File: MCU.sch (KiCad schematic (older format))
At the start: 10 parts, among them J2 Conn_01x02, J5 Conn_02x03_Odd_Even, SW2 SW_SPDT, U3 ATTINY13-20SSU

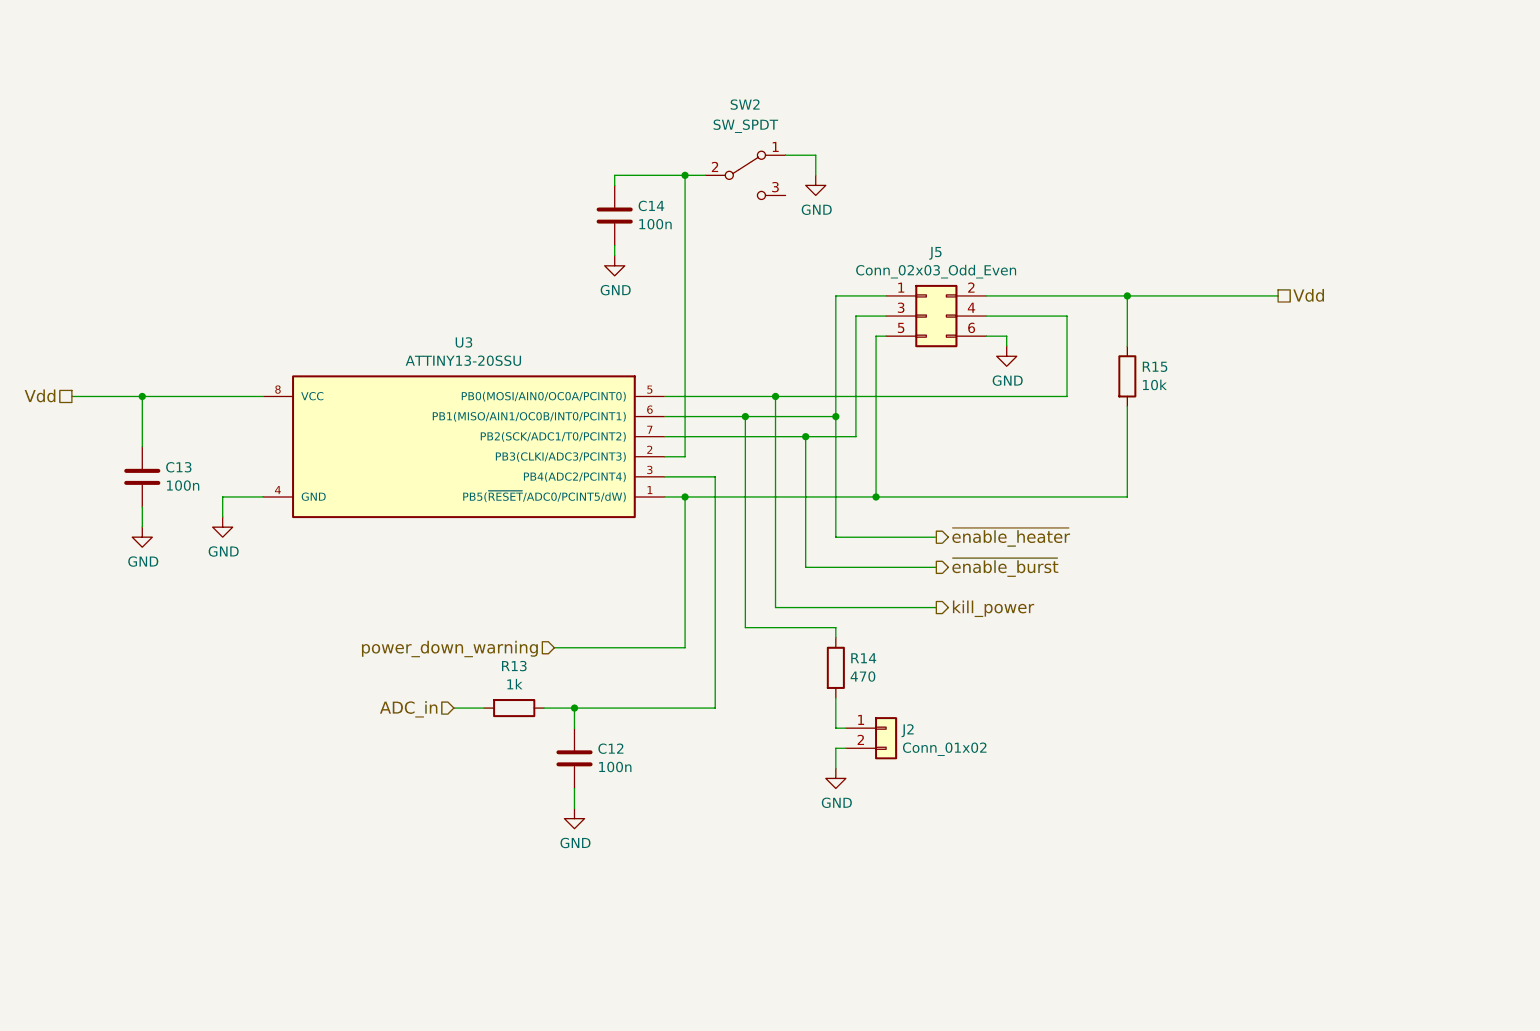
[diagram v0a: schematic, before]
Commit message: Fixed NTLJF3117P MOSFET pin layout
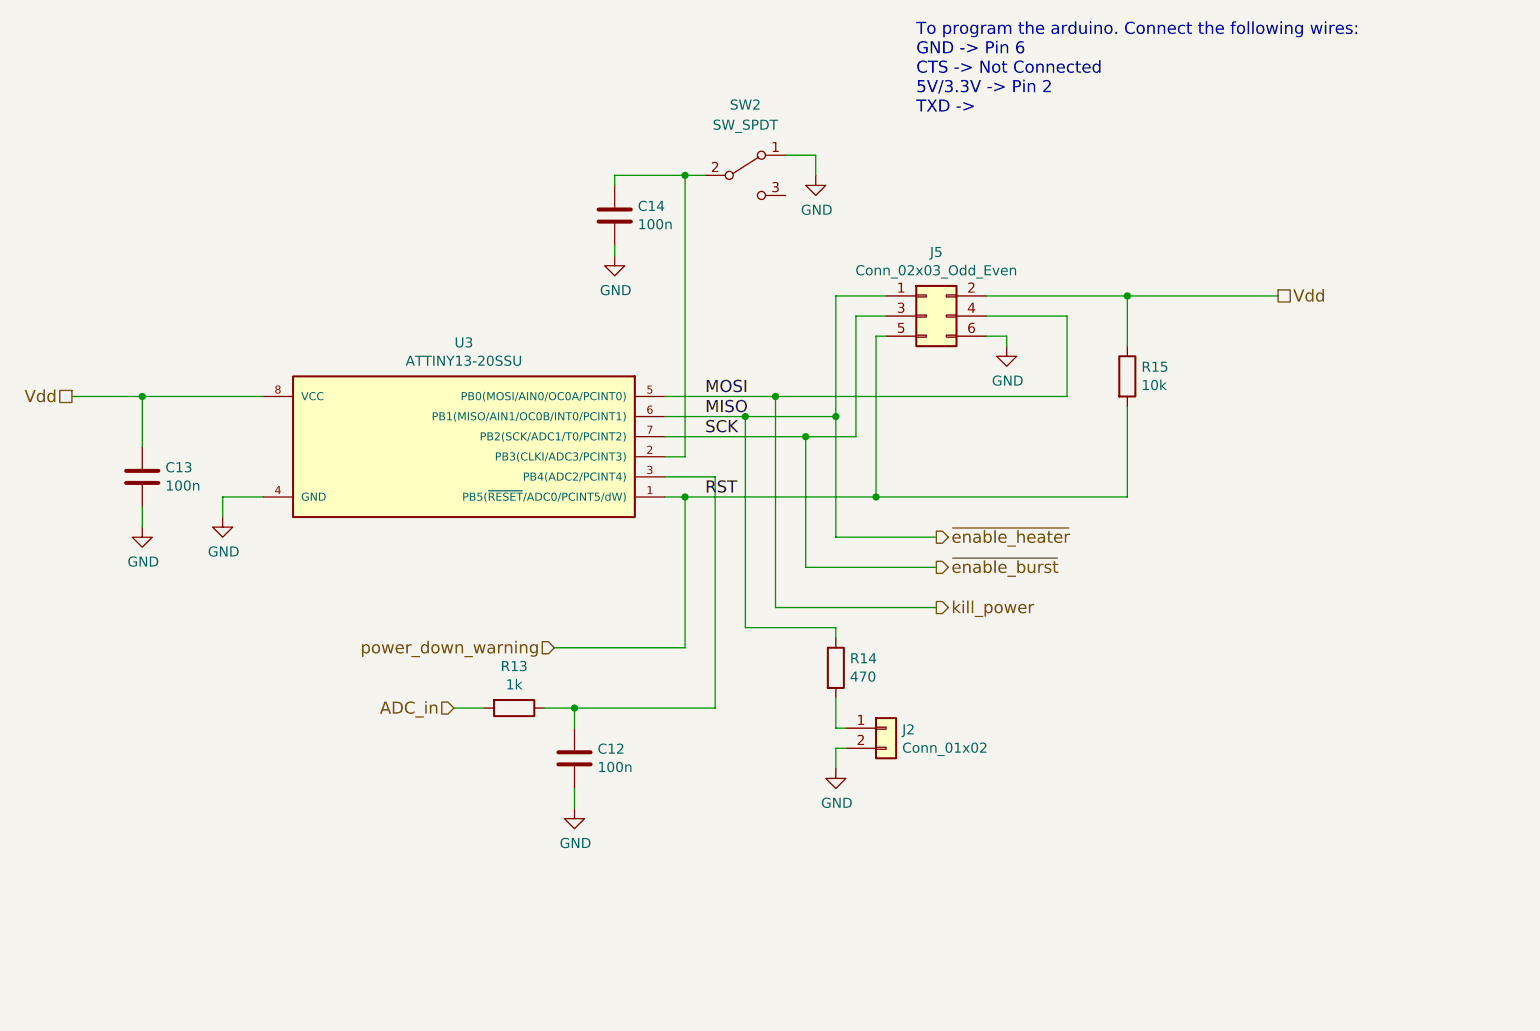
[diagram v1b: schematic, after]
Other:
- note added: "To program the arduino. Connect the following wires:\nGND -> Pin 6\nCTS -> Not Connected\n5V/3.3V -> Pin 2\nTXD ->"
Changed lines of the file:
@@
 $EndComp
 $Comp
-L GND #PWR028
+L GND #PWR027
 U 1 1 59D0B8EA
 P 5850 5050
-F 0 "#PWR028" H 5850 4800 50  0001 C CNN
+F 0 "#PWR027" H 5850 4800 50  0001 C CNN
 F 1 "GND" H 5855 4877 50  0000 C CNN
 F 2 "" H 5850 5050 50  0001 C CNN
@@
 	1    0    0    -1
 $EndComp
-Wire Wire Line
-	5250 4550 5400 4550
-Wire Wire Line
-	5700 4550 6550 4550
-Wire Wire Line
-	5850 4550 5850 4650
-Wire Wire Line
-	5850 4950 5850 5050
 $Comp
 L ATTINY13-20SSU U3
@@
 $EndComp
 $Comp
-L GND #PWR029
+L GND #PWR028
 U 1 1 59D0C06D
 P 4100 3600
-F 0 "#PWR029" H 4100 3350 50  0001 C CNN
+F 0 "#PWR028" H 4100 3350 50  0001 C CNN
 F 1 "GND" H 4105 3427 50  0000 C CNN
 F 2 "" H 4100 3600 50  0001 C CNN
@@
 	1    0    0    -1
 $EndComp
-Wire Wire Line
-	4300 3000 3350 3000
-Wire Wire Line
-	4300 3500 4100 3500
-Wire Wire Line
-	4100 3500 4100 3600
 $Comp
 L Conn_02x03_Odd_Even J5
@@
 	1    0    0    -1
 $EndComp
-Wire Wire Line
-	7400 2500 7150 2500
-Wire Wire Line
-	7150 2500 7150 3700
-Wire Wire Line
-	6300 3100 7150 3100
-Wire Wire Line
-	7400 2600 7250 2600
-Wire Wire Line
-	7250 2600 7250 3200
-Wire Wire Line
-	7250 3200 6300 3200
-Wire Wire Line
-	7400 2700 7350 2700
-Wire Wire Line
-	7350 2700 7350 3500
-Wire Wire Line
-	6300 3500 8600 3500
-Wire Wire Line
-	6300 3000 8300 3000
-Wire Wire Line
-	8300 3000 8300 2600
-Wire Wire Line
-	8300 2600 7900 2600
-$Comp
-L GND #PWR030
+$Comp
+L GND #PWR029
 U 1 1 59D0C22E
 P 8000 2750
-F 0 "#PWR030" H 8000 2500 50  0001 C CNN
+F 0 "#PWR029" H 8000 2500 50  0001 C CNN
 F 1 "GND" H 8005 2577 50  0000 C CNN
 F 2 "" H 8000 2750 50  0001 C CNN
@@
 	1    0    0    -1
 $EndComp
-Wire Wire Line
-	7900 2700 8000 2700
-Wire Wire Line
-	8000 2700 8000 2750
 Text HLabel 9350 2500 2    60   UnSpc ~ 0
 Vdd
-Wire Wire Line
-	7900 2500 9350 2500
 $Comp
 L R R15
@@
 	1    0    0    -1
 $EndComp
-Wire Wire Line
-	8600 2500 8600 2750
-Connection ~ 8600 2500
-Wire Wire Line
-	8600 3500 8600 3050
-Connection ~ 7350 3500
 $Comp
 L C C13
@@
 $EndComp
 $Comp
-L GND #PWR031
+L GND #PWR030
 U 1 1 59D0C561
 P 3700 3650
-F 0 "#PWR031" H 3700 3400 50  0001 C CNN
+F 0 "#PWR030" H 3700 3400 50  0001 C CNN
 F 1 "GND" H 3705 3477 50  0000 C CNN
 F 2 "" H 3700 3650 50  0001 C CNN
@@
 	1    0    0    -1
 $EndComp
-Wire Wire Line
-	3700 3550 3700 3650
-Wire Wire Line
-	3700 3250 3700 3000
-Connection ~ 3700 3000
 Text HLabel 7650 4050 2    60   Output ~ 0
 kill_power
 Text HLabel 5750 4250 0    60   Input ~ 0
 power_down_warning
-Wire Wire Line
-	5750 4250 6400 4250
-Wire Wire Line
-	7150 3700 7650 3700
-Connection ~ 7150 3100
-Wire Wire Line
-	6850 4050 7650 4050
-Wire Wire Line
-	6550 4550 6550 3400
-Wire Wire Line
-	6550 3400 6300 3400
-Connection ~ 5850 4550
 $Comp
 L R R14
@@
 $EndComp
 $Comp
-L GND #PWR032
+L GND #PWR031
 U 1 1 59D0EBB5
 P 7150 4850
-F 0 "#PWR032" H 7150 4600 50  0001 C CNN
+F 0 "#PWR031" H 7150 4600 50  0001 C CNN
 F 1 "GND" H 7155 4677 50  0000 C CNN
 F 2 "" H 7150 4850 50  0001 C CNN
@@
 	1    0    0    -1
 $EndComp
-Wire Wire Line
-	7150 4750 7150 4850
-Wire Wire Line
-	7150 4500 7150 4650
-Wire Wire Line
-	6700 3100 6700 4150
-Wire Wire Line
-	6700 4150 7150 4150
-Wire Wire Line
-	7150 4150 7150 4200
-Connection ~ 6700 3100
 Text HLabel 7650 3850 2    60   Output ~ 0
 ~enable_burst
-Wire Wire Line
-	7000 3200 7000 3850
-Wire Wire Line
-	7000 3850 7650 3850
-Connection ~ 7000 3200
-Wire Wire Line
-	6400 4250 6400 3500
-Connection ~ 6400 3500
 $Comp
 L SW_SPDT SW2
@@
 	1    0    0    -1
 $EndComp
-Wire Wire Line
-	6050 1900 6500 1900
-$Comp
-L GND #PWR033
+$Comp
+L GND #PWR032
 U 1 1 59D11856
 P 7050 1900
-F 0 "#PWR033" H 7050 1650 50  0001 C CNN
+F 0 "#PWR032" H 7050 1650 50  0001 C CNN
 F 1 "GND" H 7055 1727 50  0000 C CNN
 F 2 "" H 7050 1900 50  0001 C CNN
@@
 	1    0    0    -1
 $EndComp
-Wire Wire Line
-	6900 1800 7050 1800
-Wire Wire Line
-	7050 1800 7050 1900
-Wire Wire Line
-	6850 4050 6850 3000
-Connection ~ 6850 3000
-Wire Wire Line
-	6400 1900 6400 3300
-Wire Wire Line
-	6400 3300 6300 3300
 $Comp
 L Conn_01x02 J2
@@
 	1    0    0    -1
 $EndComp
-Wire Wire Line
-	7150 4650 7200 4650
-Wire Wire Line
-	7200 4750 7150 4750
 $Comp
 L C C14
@@
 	1    0    0    -1
 $EndComp
-Wire Wire Line
-	6050 1900 6050 1950
-Connection ~ 6400 1900
-$Comp
-L GND #PWR034
+$Comp
+L GND #PWR033
 U 1 1 59D1A77F
 P 6050 2300
-F 0 "#PWR034" H 6050 2050 50  0001 C CNN
+F 0 "#PWR033" H 6050 2050 50  0001 C CNN
 F 1 "GND" H 6055 2127 50  0000 C CNN
 F 2 "" H 6050 2300 50  0001 C CNN
@@
 	1    0    0    -1
 $EndComp
+Text Notes 7550 1600 0    60   ~ 0
+To program the arduino. Connect the following wires:\nGND -> Pin 6\nCTS -> Not Connected\n5V/3.3V -> Pin 2\nTXD ->
+Wire Wire Line
+	5250 4550 5400 4550
+Wire Wire Line
+	5700 4550 6550 4550
+Wire Wire Line
+	5850 4550 5850 4650
+Wire Wire Line
+	5850 4950 5850 5050
+Wire Wire Line
+	3350 3000 4300 3000
+Wire Wire Line
+	4300 3500 4100 3500
+Wire Wire Line
+	4100 3500 4100 3600
+Wire Wire Line
+	7400 2500 7150 2500
+Wire Wire Line
+	7150 2500 7150 3700
+Wire Wire Line
+	6300 3100 7150 3100
+Wire Wire Line
+	7400 2600 7250 2600
+Wire Wire Line
+	7250 2600 7250 3200
+Wire Wire Line
+	7250 3200 6300 3200
+Wire Wire Line
+	7400 2700 7350 2700
+Wire Wire Line
+	7350 2700 7350 3500
+Wire Wire Line
+	6300 3500 8600 3500
+Wire Wire Line
+	6300 3000 8300 3000
+Wire Wire Line
+	8300 3000 8300 2600
+Wire Wire Line
+	8300 2600 7900 2600
+Wire Wire Line
+	7900 2700 8000 2700
+Wire Wire Line
+	8000 2700 8000 2750
+Wire Wire Line
+	8600 2500 8600 2750
+Connection ~ 8600 2500
+Wire Wire Line
+	8600 3500 8600 3050
+Connection ~ 7350 3500
+Wire Wire Line
+	3700 3550 3700 3650
+Wire Wire Line
+	3700 3250 3700 3000
+Connection ~ 3700 3000
+Wire Wire Line
+	5750 4250 6400 4250
+Wire Wire Line
+	7150 3700 7650 3700
+Connection ~ 7150 3100
+Wire Wire Line
+	6850 4050 7650 4050
+Wire Wire Line
+	6550 4550 6550 3400
+Wire Wire Line
+	6550 3400 6300 3400
+Connection ~ 5850 4550
+Wire Wire Line
+	7150 4750 7150 4850
+Wire Wire Line
+	7150 4500 7150 4650
+Wire Wire Line
+	6700 3100 6700 4150
+Wire Wire Line
+	6700 4150 7150 4150
+Wire Wire Line
+	7150 4150 7150 4200
+Connection ~ 6700 3100
+Wire Wire Line
+	7000 3200 7000 3850
+Wire Wire Line
+	7000 3850 7650 3850
+Connection ~ 7000 3200
+Wire Wire Line
+	6400 4250 6400 3500
+Connection ~ 6400 3500
+Wire Wire Line
+	6050 1900 6500 1900
+Wire Wire Line
+	6900 1800 7050 1800
+Wire Wire Line
+	7050 1800 7050 1900
+Wire Wire Line
+	6850 4050 6850 3000
+Connection ~ 6850 3000
+Wire Wire Line
+	6400 1900 6400 3300
+Wire Wire Line
+	6400 3300 6300 3300
+Wire Wire Line
+	7150 4650 7200 4650
+Wire Wire Line
+	7200 4750 7150 4750
+Wire Wire Line
+	6050 1900 6050 1950
+Connection ~ 6400 1900
 Wire Wire Line
 	6050 2300 6050 2250
+Wire Wire Line
+	7900 2500 9350 2500
+Text Label 6500 3500 0    60   ~ 0
+RST
+Text Label 6500 3000 0    60   ~ 0
+MOSI
+Text Label 6500 3100 0    60   ~ 0
+MISO
+Text Label 6500 3200 0    60   ~ 0
+SCK
 $EndSCHEMATC
